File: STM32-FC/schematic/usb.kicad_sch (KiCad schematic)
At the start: 27 parts, among them J2 USB_C_USB2.0_14P, J3 SM06B-GHS-TBT, U1 USBLC6-2SC6, U2 TPS62840, U3 TPS62840, U4 TPS62840

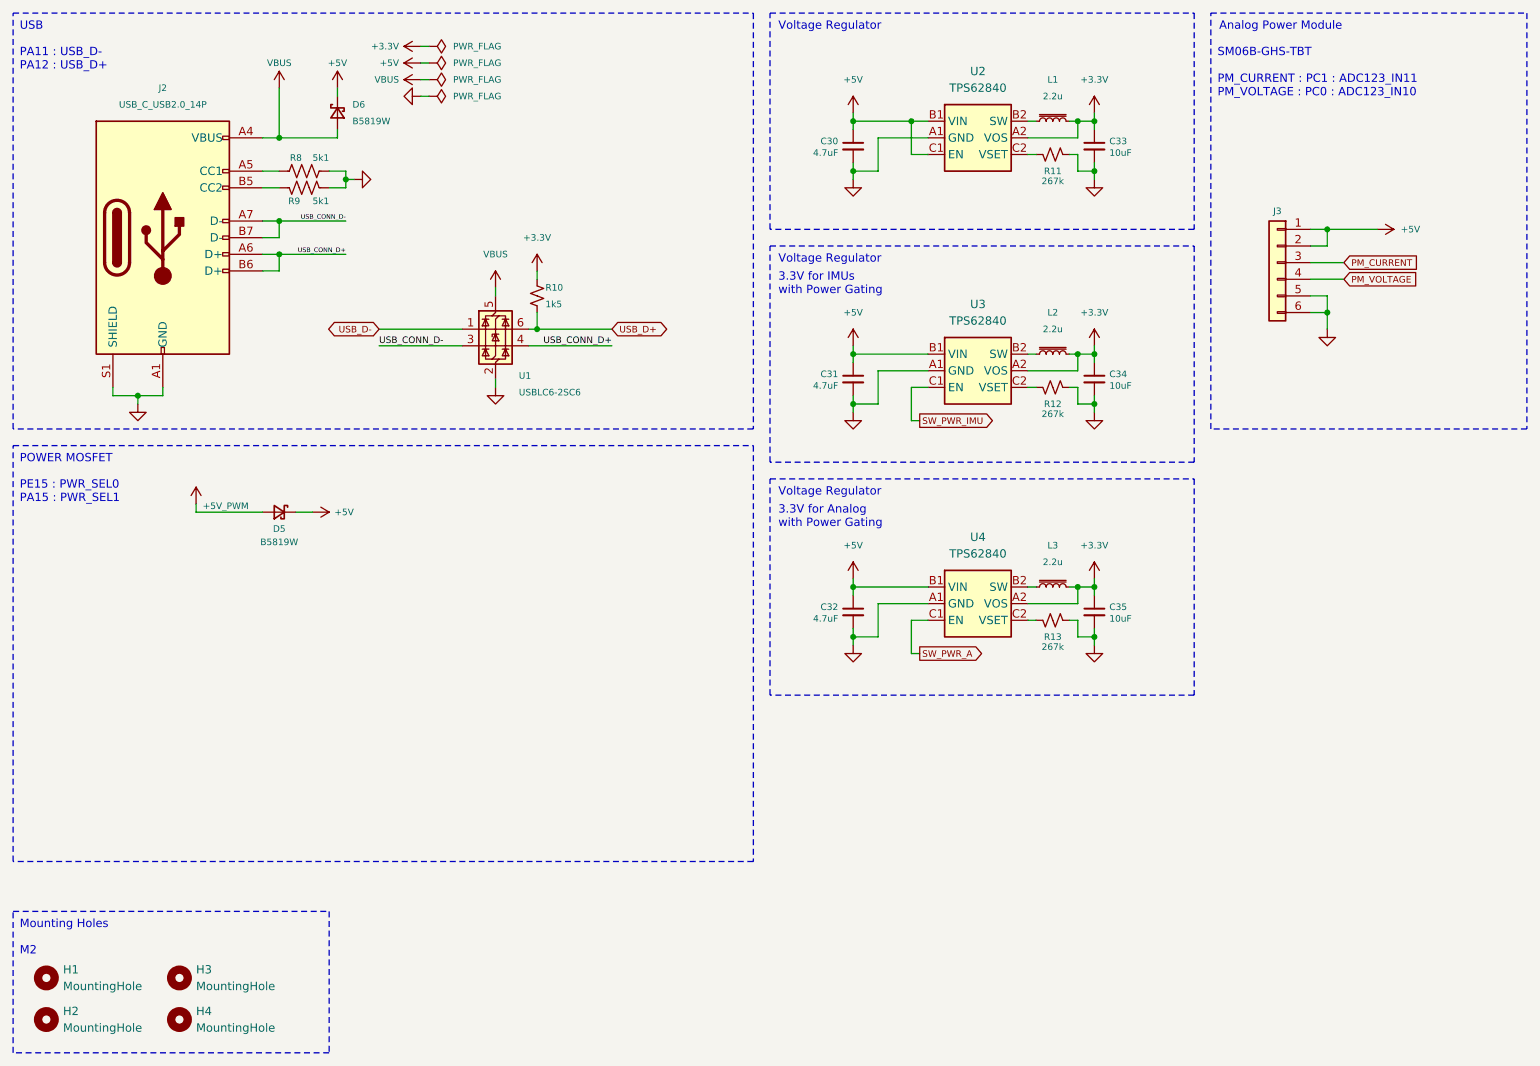
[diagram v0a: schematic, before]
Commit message: fix : BMM350 power 1.8V and add dc2dc converter for 1.8V
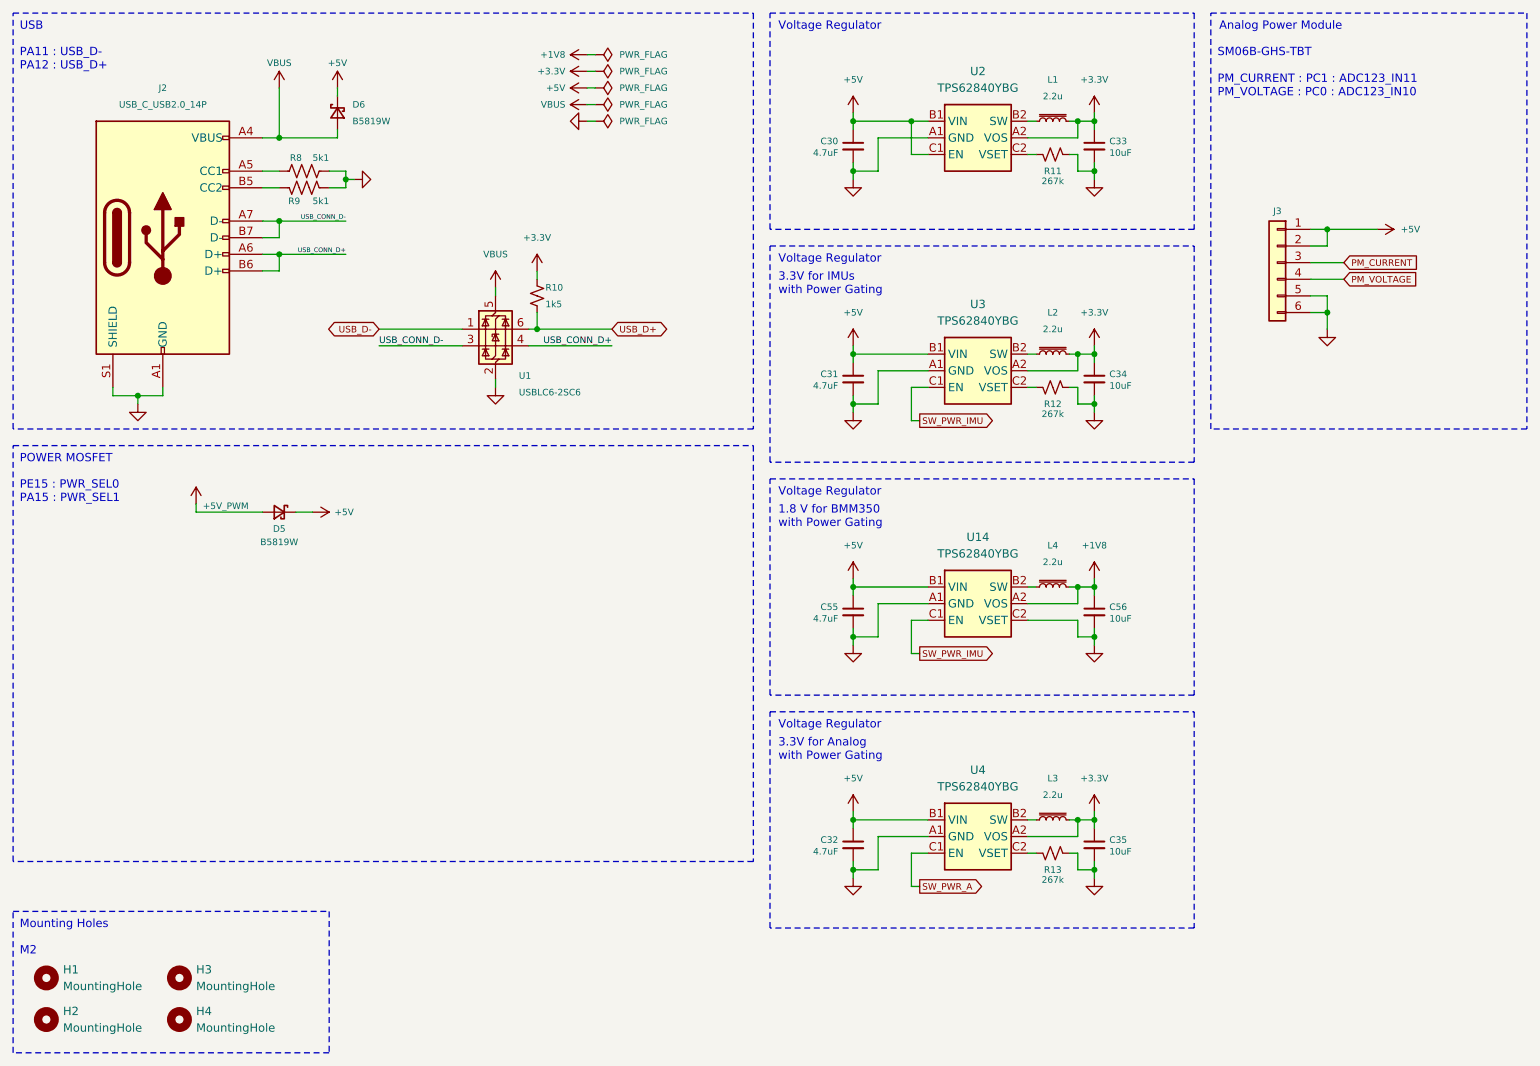
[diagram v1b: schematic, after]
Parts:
- added C55: 4.7uF, Capacitor_SMD:C_0402_1005Metric, symbol Device:C_Small
- added C56: 10uF, Capacitor_SMD:C_0402_1005Metric, symbol Device:C_Small
- added L4: 2.2u, VLS201610ET-2R2M:VLS201610ET-2R2M, symbol Device:L_Iron_Small
- added U14: TPS62840YBG, Package_BGA:Texas_DSBGA-6_0.855x1.255mm_Layout2x3_P0.4mm_LevelC, symbol TPS62840:TPS62840YBG
- U2, U3, U4: value TPS62840 -> TPS62840YBG
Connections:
- net +5V: now also C55.1, U14.B1 (VIN)
- net GND: now also C55.2, C56.2, U14.A1 (GND), U14.C2 (VSET)
- net SW_PWR_IMU: now also U14.C1 (EN)
- new net: L4.1, U14.B2 (SW)
- new net +1V8: C56.1, L4.2, U14.A2 (VOS)
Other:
- note added: "1.8 V for BMM350 with Power Gating"
- moved on the sheet: C32, C35, L3, R13, U4

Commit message: update : BOM and minor fix
- remove : DC2DC for analog
- change : JST SM conn. to BM
- change : ELRS conn. to JST XH (instead of JST SM)
- update : BOM List
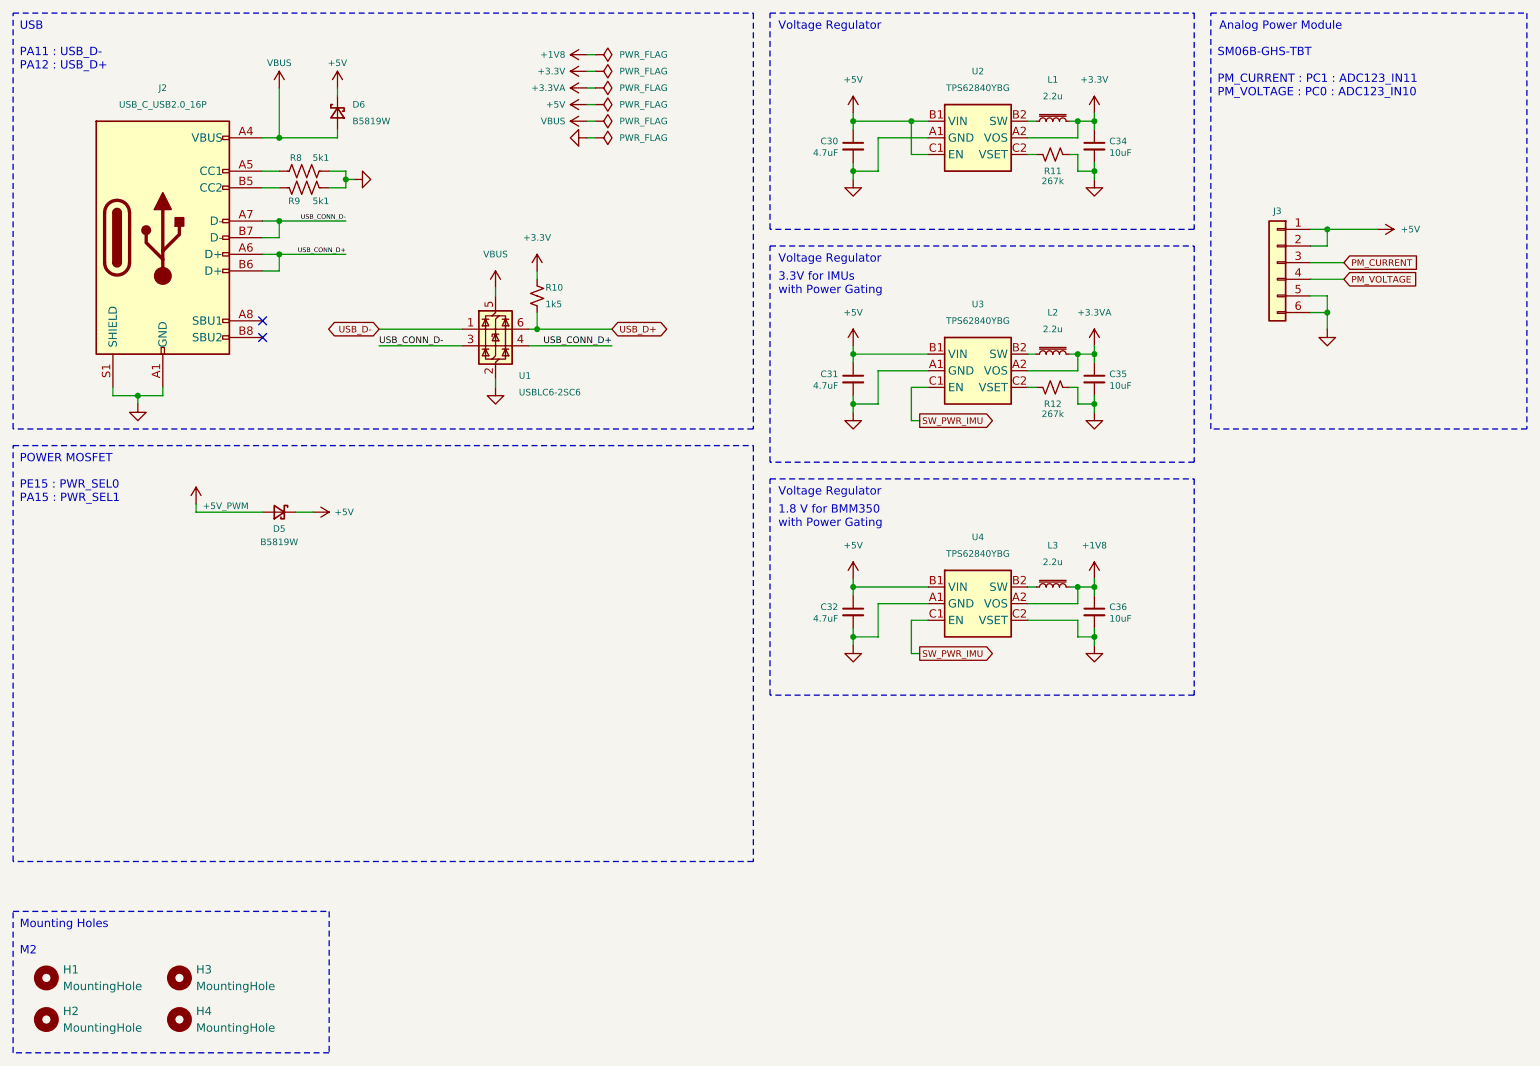
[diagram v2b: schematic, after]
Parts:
- removed C32: 4.7uF, Capacitor_SMD:C_0402_1005Metric, symbol Device:C_Small
- removed C35: 10uF, Capacitor_SMD:C_0402_1005Metric, symbol Device:C_Small
- removed J2: USB_C_USB2.0_14P, Connector_USB:USB_C_Receptacle_GCT_USB4110, symbol Connector:USB_C_Receptacle_USB2.0_14P
- removed L3: 2.2u, VLS201610ET-2R2M:VLS201610ET-2R2M, symbol Device:L_Iron_Small
- removed R13: 267k, Resistor_SMD:R_0402_1005Metric, symbol Device:R_Small_US
- removed U4: TPS62840YBG, Package_BGA:Texas_DSBGA-6_0.855x1.255mm_Layout2x3_P0.4mm_LevelC, symbol TPS62840:TPS62840YBG
- added J2: USB_C_USB2.0_16P, Connector_USB:USB_C_Receptacle_GCT_USB4105-xx-A_16P_TopMnt_Horizontal, symbol Connector:USB_C_Receptacle_USB2.0_16P
- J3: value SM06B-GHS-TBT -> BM06B-GHS-TBT; footprint Connector_JST:JST_GH_SM06B-GHS-TB_1x06-1MP_P1.25mm_Horizontal -> Connector_JST:JST_GH_BM06B-GHS-TBT_1x06-1MP_P1.25mm_Vertical; LCSC C133065 -> C189892
- renumbered C55 to C32, C33 to C34, C34 to C35, C56 to C36, L4 to L3, U14 to U4
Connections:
- net +3.3V: no longer C35.1, L2.2, U3.A2 (VOS)
- net GND: now also J2.A1 (GND), J2.A12 (GND), J2.B1 (GND), J2.B12 (GND), J2.S1 (SHIELD)
- net USB_CONN_D+: now also J2.A6 (D+), J2.B6 (D+)
- net USB_CONN_D-: now also J2.A7 (D-), J2.B7 (D-)
- net VBUS: now also J2.A4 (VBUS), J2.A9 (VBUS), J2.B4 (VBUS), J2.B9 (VBUS)
- net at R9.1: now also J2.B5 (CC2)
- net at R8.1: now also J2.A5 (CC1)
- new net +3.3VA: C35.1, L2.2, U3.A2 (VOS)
- no-connect marks 0 -> 2
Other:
- note removed: "3.3V for Analog with Power Gating"
